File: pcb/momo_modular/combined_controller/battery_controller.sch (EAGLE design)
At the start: 34 parts, among them U1 XRP7659, U2 MAX1555, U3 MCP1702, U4 PIC24F16KA101-X_PSSOP, U5 FLASH8MSOP8

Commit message: Finished next version of hardware.  Working on automatic BOM generation for purchasing.
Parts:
- added JP2: MOMO-EDGE-6F, components:MOMO-EDGE-6F
- added Q1, Q2: P-MOSFET, components:P-MOSFET
- added R12, R13: 100K, rcl:R-US_R0603
- C1, C2, C5: DIGIKEY-PN (none) -> 445-1265-1-ND
- C13, C14: DIGIKEY-PN (none) -> 445-1238-1-ND
- C3, C6: DIGIKEY-PN (none) -> 587-2985-1-ND
- C4: DIGIKEY-PN (none) -> 445-1260-1-ND
- C7, C8: DIGIKEY-PN (none) -> 445-4114-1-ND
- D1: DIGIKEY-PN (none) -> SS2P3-M3/84AGICT-ND
- JP1: value MOMO-VERT-8M -> MOMO-VERT-6M; device components:MOMO-VERT-8M -> components:MOMO-VERT-6M; DIGIKEY-PN (none) -> 609-3263-ND
- JP3: value MOMO-EDGE-8F -> (none); device components:MOMO-EDGE-8F -> pinhead:PINHD-1X1
- L1: DIGIKEY-PN (none) -> 587-2100-1-ND
- R1, R2, R3: DIGIKEY-PN (none) -> P10.0KHCT-ND
- R10: value 9.7k -> 10k; DIGIKEY-PN (none) -> P10.0KHCT-ND
- R11: DIGIKEY-PN (none) -> 641-1332-1-ND
- R4: DIGIKEY-PN (none) -> P0.0GCT-ND
- R5: value 10k -> 10K; device rcl:R-US_R0402 -> rcl:R-US_R0603; DIGIKEY-PN (none) -> P10.0KHCT-ND
- R6: DIGIKEY-PN (none) -> P100KHCT-ND
- R7, R8: value 500K -> 510K; DIGIKEY-PN (none) -> P510KHCT-ND
- R9: value 50k -> 51k; DIGIKEY-PN (none) -> P510KHCT-ND
- U$1, U$2: DIGIKEY-PN (none) -> A19450-ND
- U1: DIGIKEY-PN (none) -> 1016-1751-1-ND
- U2: DIGIKEY-PN (none) -> MAX1555EZK+TCT-ND
- U3: DIGIKEY-PN (none) -> MCP1702T-2802E/CBCT-ND
- U5: DIGIKEY-PN (none) -> M25PX80-VMN6TPCT-ND
- XTAL1: DIGIKEY-PN (none) -> 300-8814-1-ND
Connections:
- net N$6 renamed VBAT_SAMP
- net N$9 renamed BUCK_EN
- new net MEM_POW: C5.1, U4.U1TX/INT0/CN23/RB7, U5.RST, U5.VCC, U5.WPROT
- new net N$3: Q1.DRAIN, R7.2
- new net SAMP_EN: Q1.GATE, R12.2, U4.PGD2/AN1/VREF-/CN3/RA1
- new net VCCIO: JP1.2.8V, JP2.2.8V, Q2.DRAIN
- new net VCC_EN: Q2.GATE, R13.2, U4.PGC2/AN0/VREF+/CN2/RA0
- net +18V: now also U$1.GND; no longer U$1.3.8V
- net GND: now also JP2.GND, R13.1, U$1.3.8V, U$2.3.8V; no longer JP1.PGND, JP3.GND, JP3.PGND, U$1.GND, U$2.GND
- net ICLK: now also JP2.CLK, U4.PGC1/AN3/C1INC/C2INA/U2RX/U2BCLK/CN5/RB1; no longer JP3.CLK
- net IDAT: now also JP2.DAT, U4.PGD1/AN2/C1IND/C2INB/U2TX/CN4/RB0; no longer JP3.DAT
- net IRQ: now also JP2.ALRM; no longer JP3.ALRM
- net N$15: now also JP3.1
- net V+: now also JP2.4V, Q1.SOURCE, R12.1, U$2.GND; no longer JP3.4V, R7.2, U$2.3.8V
- net VCCINT: now also Q2.SOURCE; no longer C5.1, JP1.2.8V, JP3.2.8V, U5.RST, U5.VCC, U5.WPROT
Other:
- note added: "9/17/13"
- note added: "Combined battery, solar and external power."
- note removed: "5/12/13"
- note removed: "Version 1"
- moved on the sheet: C13, C14, C2, C3, C4, C5, C6, C7, C8, C9, L1, R10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

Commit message: Finished versions of core MoMo hardware along with python tools to autogenerate bill of materials files for each board.
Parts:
- C3, C6: DIGIKEY-PN 587-2985-1-ND -> (none); DIGIKEY-PN-BATT (none) -> 587-2985-1-ND; DIGIKEY-PN-EXTPOWER (none) -> 587-2985-1-ND
- C4: DIGIKEY-PN 445-1260-1-ND -> (none); DIGIKEY-PN-BATT (none) -> 445-1260-1-ND; DIGIKEY-PN-EXTPOWER (none) -> 445-1260-1-ND
- C7, C8: DIGIKEY-PN 445-4114-1-ND -> (none); DIGIKEY-PN-BATT (none) -> 445-4114-1-ND; DIGIKEY-PN-SOLAR (none) -> 445-4114-1-ND
- C9: DIGIKEY-PN (none) -> 445-4114-1-ND
- D1: DIGIKEY-PN SS2P3-M3/84AGICT-ND -> (none); DIGIKEY-PN-BATT (none) -> SS2P3-M3/84AGICT-ND; DIGIKEY-PN-EXTPOWER (none) -> SS2P3-M3/84AGICT-ND
- L1: DIGIKEY-PN 587-2100-1-ND -> (none); DIGIKEY-PN-BATT (none) -> 587-2100-1-ND; DIGIKEY-PN-EXTPOWER (none) -> 587-2100-1-ND
- R10: DIGIKEY-PN P10.0KHCT-ND -> (none); DIGIKEY-PN-BATT (none) -> P10.0KHCT-ND; DIGIKEY-PN-EXTPOWER (none) -> P13.0KHCT-ND
- R11: DIGIKEY-PN 641-1332-1-ND -> (none); DIGIKEY-PN-SOLAR (none) -> 641-1332-1-ND
- R4: DIGIKEY-PN P0.0GCT-ND -> (none); DIGIKEY-PN-EXTPOWER (none) -> P0.0GCT-ND
- R6: DIGIKEY-PN P100KHCT-ND -> (none); DIGIKEY-PN-BATT (none) -> P100KHCT-ND; DIGIKEY-PN-EXTPOWER (none) -> P100KHCT-ND
- R9: DIGIKEY-PN P510KHCT-ND -> (none); DIGIKEY-PN-BATT (none) -> P510KHCT-ND; DIGIKEY-PN-EXTPOWER (none) -> P510KHCT-ND
- U1: DIGIKEY-PN 1016-1751-1-ND -> (none); DIGIKEY-PN-BATT (none) -> 1016-1751-1-ND; DIGIKEY-PN-EXTPOWER (none) -> 1016-1751-1-ND
- U2: DIGIKEY-PN MAX1555EZK+TCT-ND -> (none); DIGIKEY-PN-BATT (none) -> MAX1555EZK+TCT-ND; DIGIKEY-PN-SOLAR (none) -> MAX1555EZK+TCT-ND
- U4: BATT (none) -> ASSY-VARIANT; DIGIKEY-PN (none) -> PIC24F16KA101-I/SS-ND; EXTPOWER (none) -> ASSY-VARIANT; SOLAR (none) -> ASSY-VARIANT
- renumbered U$1 to JP5, U$2 to JP4

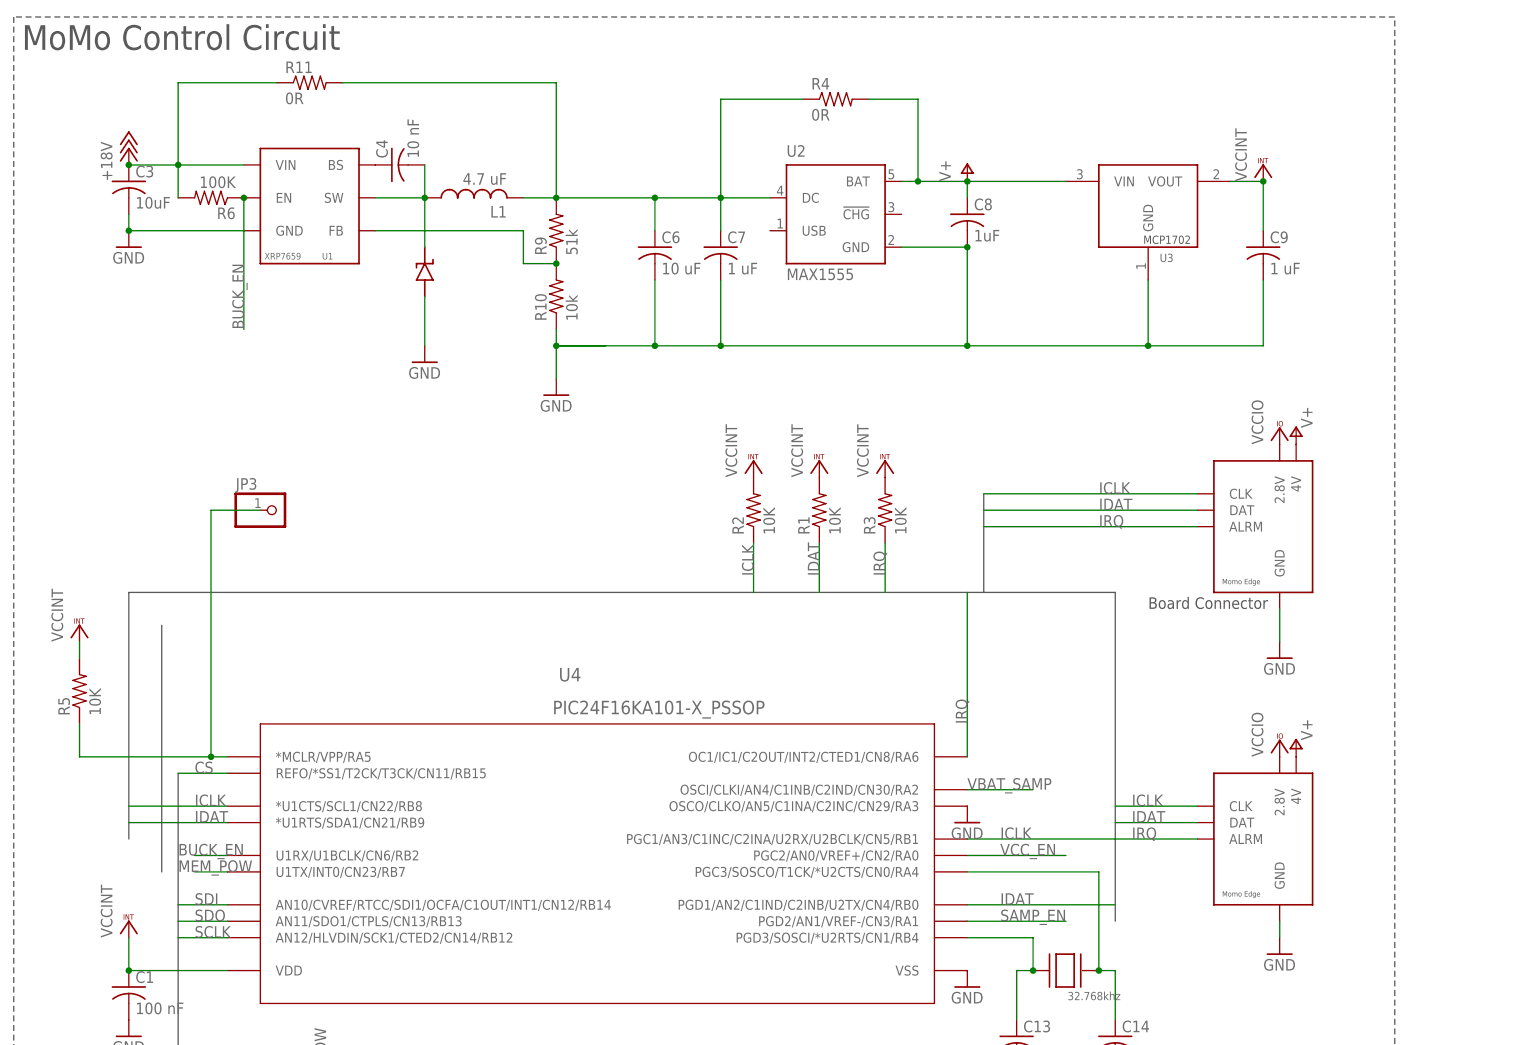
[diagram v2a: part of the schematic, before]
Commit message: Revised combined controller board into what should be the final version.  Added a current sense circuit to track battery charging, relaid traces out and swapped out the charger IC for a much cheaper one with a disable signal.
Added a schottky diode on the input in all assembly variants to prevent reverse polarity charging and to prevent discharging into the charger if the charger loses power.
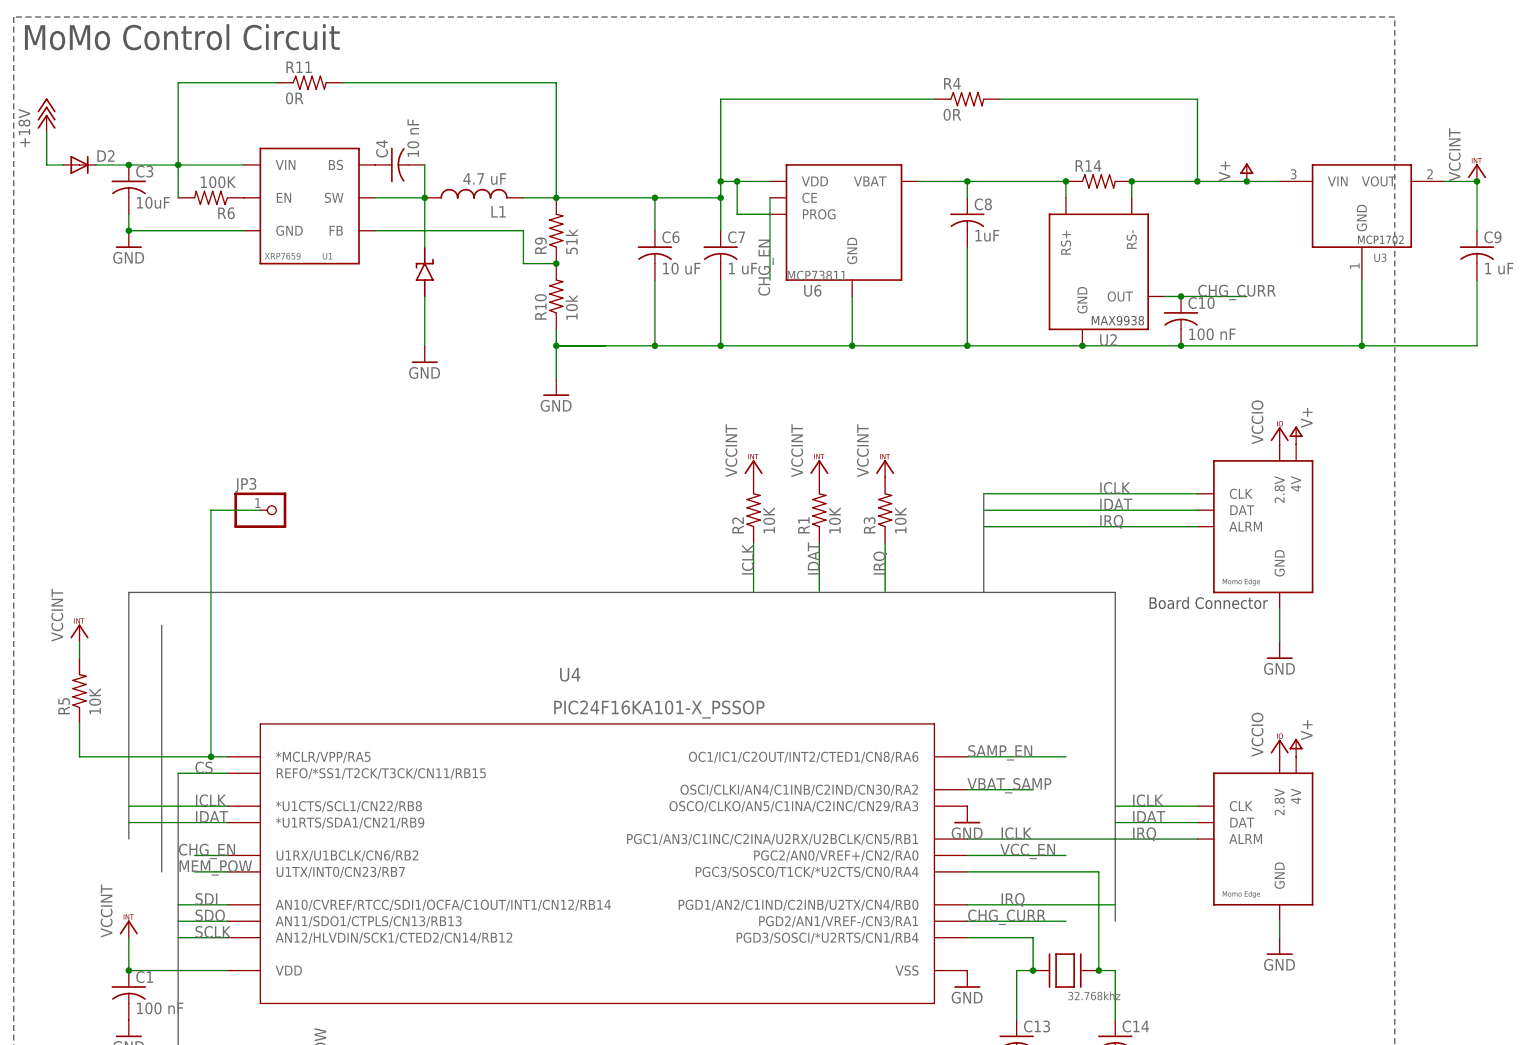
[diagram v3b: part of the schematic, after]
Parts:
- added C10: 100 nF, rcl:C-USC0402
- added D2: (no value), diode:DIODE-DO214AC
- added R14: (no value), rcl:R-US_R0603
- added U6: MCP73811, components:MCP73811
- R11: DIGIKEY-PN-SOLAR 641-1332-1-ND -> P0.0GCT-ND
- U2: value MAX1555 -> MAX9938; device maxim:MAX1555 -> components:MAX9938; DIGIKEY-PN-BATT MAX1555EZK+TCT-ND -> MAX9938FEUK+TCT-ND; DIGIKEY-PN-SOLAR MAX1555EZK+TCT-ND -> MAX9938FEUK+TCT-ND
- renumbered XTAL1 to XT1
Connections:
- new net CHG_CURR: C10.1, U2.OUT, U4.PGD2/AN1/VREF-/CN3/RA1
- new net CHG_EN: U4.U1RX/U1BCLK/CN6/RB2, U6.CE
- new net N$1: C3.1, D2.C, R11.1, R6.2, U1.VIN
- new net N$4: C8.1, R14.1, U2.RS+, U6.VBAT
- net +18V: now also D2.A; no longer C3.1, R11.1, R6.2, U1.VIN
- net BUCK_EN: no longer U4.U1RX/U1BCLK/CN6/RB2
- net GND: now also C10.2, U6.GND
- net IDAT: no longer U4.PGD1/AN2/C1IND/C2INB/U2TX/CN4/RB0
- net IRQ: now also U4.PGD1/AN2/C1IND/C2INB/U2TX/CN4/RB0; no longer U4.OC1/IC1/C2OUT/INT2/CTED1/CN8/RA6
- net N$5: now also U6.PROG, U6.VDD; no longer U2.DC
- net SAMP_EN: now also U4.OC1/IC1/C2OUT/INT2/CTED1/CN8/RA6; no longer U4.PGD2/AN1/VREF-/CN3/RA1
- net V+: now also R14.2, U2.RS-; no longer C8.1, U2.BAT
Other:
- moved on the sheet: C9, R4, U3

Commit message: Moved pcb parts around on the controller to facilitate assembly.
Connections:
- net CHG_EN: now also U4.OC1/IC1/C2OUT/INT2/CTED1/CN8/RA6; no longer U4.U1RX/U1BCLK/CN6/RB2
- net SAMP_EN: now also U4.U1RX/U1BCLK/CN6/RB2; no longer U4.OC1/IC1/C2OUT/INT2/CTED1/CN8/RA6
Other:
- note added: "10/7/13"
- note removed: "9/17/13"
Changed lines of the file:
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@@
 <setting verticaltext="up"/>
 </settings>
-<grid distance="0.1" unitdist="inch" unit="inch" style="lines" multiple="1" display="no" altdistance="0.01" altunitdist="inch" altunit="inch"/>
+<grid distance="0.025" unitdist="inch" unit="inch" style="lines" multiple="1" display="no" altdistance="0.01" altunitdist="inch" altunit="inch"/>
 <layers>
 <layer number="1" name="Top" color="4" fill="1" visible="no" active="no"/>
@@
 <plain>
 <wire x1="-226.06" y1="127" x2="-226.06" y2="-111.76" width="0.1524" layer="97" style="longdash"/>
-<wire x1="-226.06" y1="-111.76" x2="-12.7" y2="-111.76" width="0.1524" layer="97" style="longdash"/>
-<wire x1="-12.7" y1="-111.76" x2="-12.7" y2="127" width="0.1524" layer="97" style="longdash"/>
-<wire x1="-12.7" y1="127" x2="-226.06" y2="127" width="0.1524" layer="97" style="longdash"/>
+<wire x1="-226.06" y1="-111.76" x2="10.16" y2="-111.76" width="0.1524" layer="97" style="longdash"/>
+<wire x1="10.16" y1="-111.76" x2="10.16" y2="127" width="0.1524" layer="97" style="longdash"/>
+<wire x1="10.16" y1="127" x2="-226.06" y2="127" width="0.1524" layer="97" style="longdash"/>
 <wire x1="-223.52" y1="-109.22" x2="-223.52" y2="-96.52" width="0.3048" layer="97"/>
 <wire x1="-223.52" y1="-96.52" x2="-223.52" y2="-91.44" width="0.3048" layer="97"/>
@@
 <text x="-50.8" y="35.56" size="1.778" layer="97">Board Connector</text>
 <text x="-209.55" y="-85.09" size="1.778" layer="97">MoMo Control Module</text>
-<text x="-209.55" y="-90.17" size="1.778" layer="97">9/17/13</text>
+<text x="-209.55" y="-90.17" size="1.778" layer="97">10/7/13</text>
 <text x="-224.79" y="121.92" size="3.81" layer="97">MoMo Control Circuit</text>
-<text x="-208.28" y="-104.14" size="1.778" layer="97">Combined battery, solar
+<text x="-209.55" y="-101.6" size="1.778" layer="97">Combined battery, solar
 and external power.</text>
 </plain>
@@
 </segment>
 <segment>
-<pinref part="U4" gate="A" pin="OC1/IC1/C2OUT/INT2/CTED1/CN8/RA6"/>
-<wire x1="-78.74" y1="12.7" x2="-63.5" y2="12.7" width="0.1524" layer="91"/>
-<label x="-78.74" y="12.7" size="1.778" layer="95"/>
+<pinref part="U4" gate="A" pin="U1RX/U1BCLK/CN6/RB2"/>
+<wire x1="-193.04" y1="-2.54" x2="-198.12" y2="-2.54" width="0.1524" layer="91"/>
+<label x="-200.66" y="-2.54" size="1.778" layer="95"/>
 </segment>
 </net>
@@
 </segment>
 <segment>
-<pinref part="U4" gate="A" pin="U1RX/U1BCLK/CN6/RB2"/>
-<wire x1="-193.04" y1="-2.54" x2="-198.12" y2="-2.54" width="0.1524" layer="91"/>
-<label x="-200.66" y="-2.54" size="1.778" layer="95"/>
-</segment>
-</net>
+<pinref part="U4" gate="A" pin="OC1/IC1/C2OUT/INT2/CTED1/CN8/RA6"/>
+<wire x1="-78.74" y1="12.7" x2="-63.5" y2="12.7" width="0.1524" layer="91"/>
+<label x="-78.74" y="12.7" size="1.778" layer="95"/>
+</segment>
+</net>

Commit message: updated board to have correct value for 51K resistor (wrong digikey part number)
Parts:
- R9: DIGIKEY-PN-BATT P510KHCT-ND -> P51.0KHCT-ND; DIGIKEY-PN-EXTPOWER P510KHCT-ND -> P51.0KHCT-ND
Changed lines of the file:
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@@
 <setting verticaltext="up"/>
 </settings>
-<grid distance="0.025" unitdist="inch" unit="inch" style="lines" multiple="1" display="no" altdistance="0.01" altunitdist="inch" altunit="inch"/>
+<grid distance="0.1" unitdist="inch" unit="inch" style="lines" multiple="1" display="no" altdistance="0.01" altunitdist="inch" altunit="inch"/>
 <layers>
 <layer number="1" name="Top" color="4" fill="1" visible="no" active="no"/>
@@
 <part name="GND10" library="supply1" deviceset="GND" device=""/>
 <part name="R9" library="rcl" deviceset="R-US_" device="R0603" value="51k">
-<attribute name="DIGIKEY-PN-BATT" value="P510KHCT-ND"/>
-<attribute name="DIGIKEY-PN-EXTPOWER" value="P510KHCT-ND"/>
+<attribute name="DIGIKEY-PN-BATT" value="P51.0KHCT-ND"/>
+<attribute name="DIGIKEY-PN-EXTPOWER" value="P51.0KHCT-ND"/>
 </part>
 <part name="R10" library="rcl" deviceset="R-US_" device="R0603" value="10k">

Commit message: Added ability to specify FOOTPRINTS and DESCRIPTIONS using Eagle attributes and have the production scripts pick those up and use them in producing BOM descriptions and footprints.
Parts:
- L1: value 4.7 uF -> 4.7 uH
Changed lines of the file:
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@@
 <attribute name="DIGIKEY-PN-EXTPOWER" value="P100KHCT-ND"/>
 </part>
-<part name="L1" library="components" deviceset="NR6028-INDUCTOR" device="" value="4.7 uF">
+<part name="L1" library="components" deviceset="NR6028-INDUCTOR" device="" value="4.7 uH">
 <attribute name="DIGIKEY-PN-BATT" value="587-2100-1-ND"/>
 <attribute name="DIGIKEY-PN-EXTPOWER" value="587-2100-1-ND"/>
